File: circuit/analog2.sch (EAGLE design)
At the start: 65 parts, among them IC1 OP07C, IC2 74HC4052D, IC3 OP07C

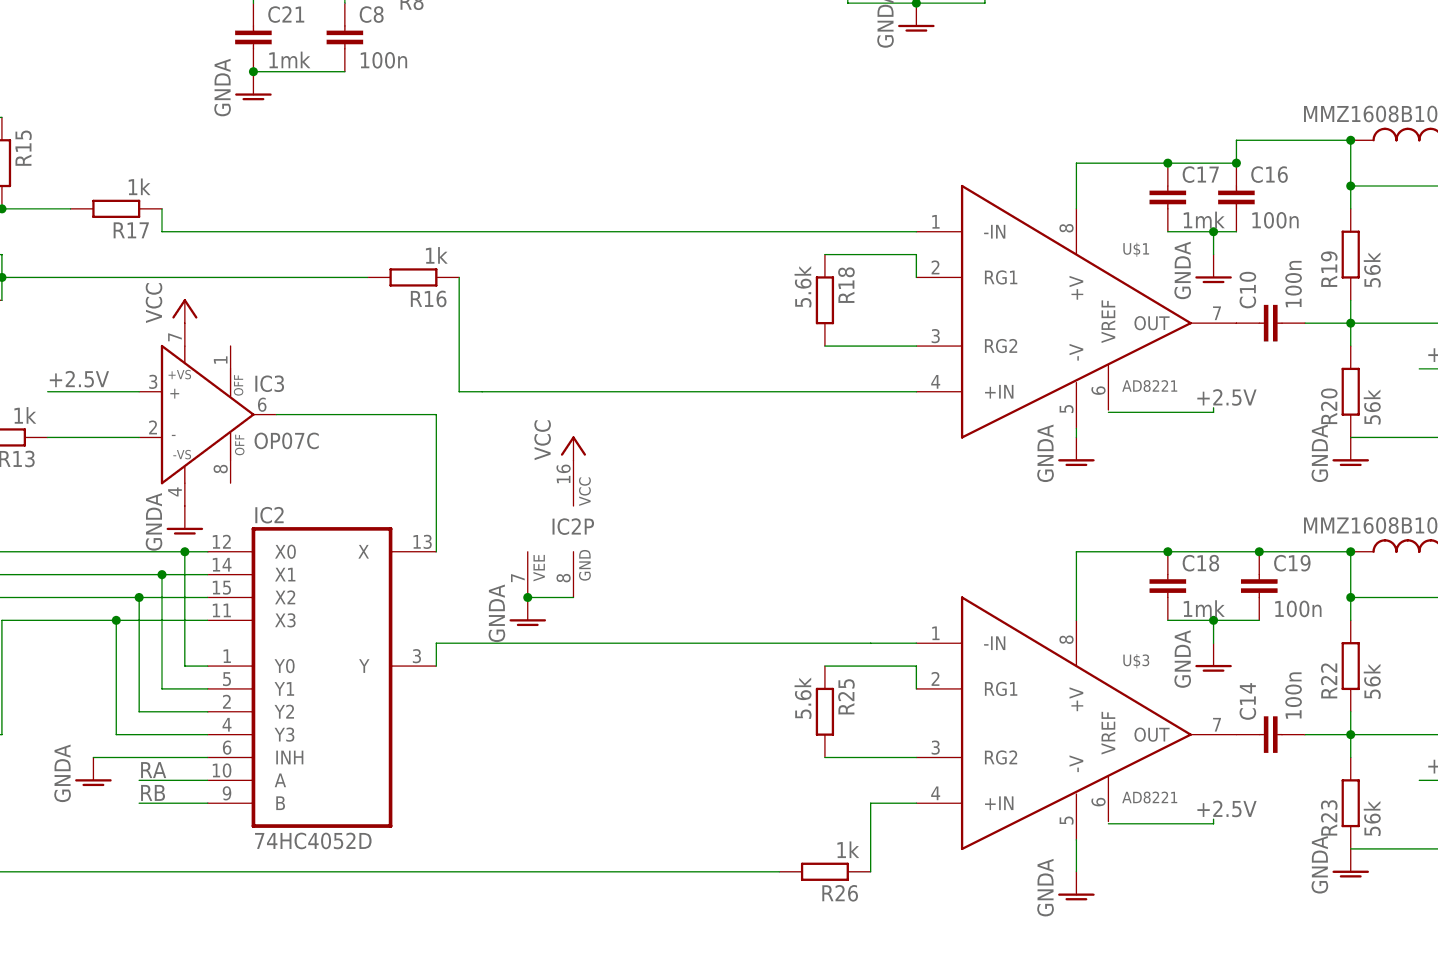
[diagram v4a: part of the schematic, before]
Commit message: - черновой вариант разводки, не проверяли как земля разведенна. Не добавляли пинов, чтобы осциллографом цепляться
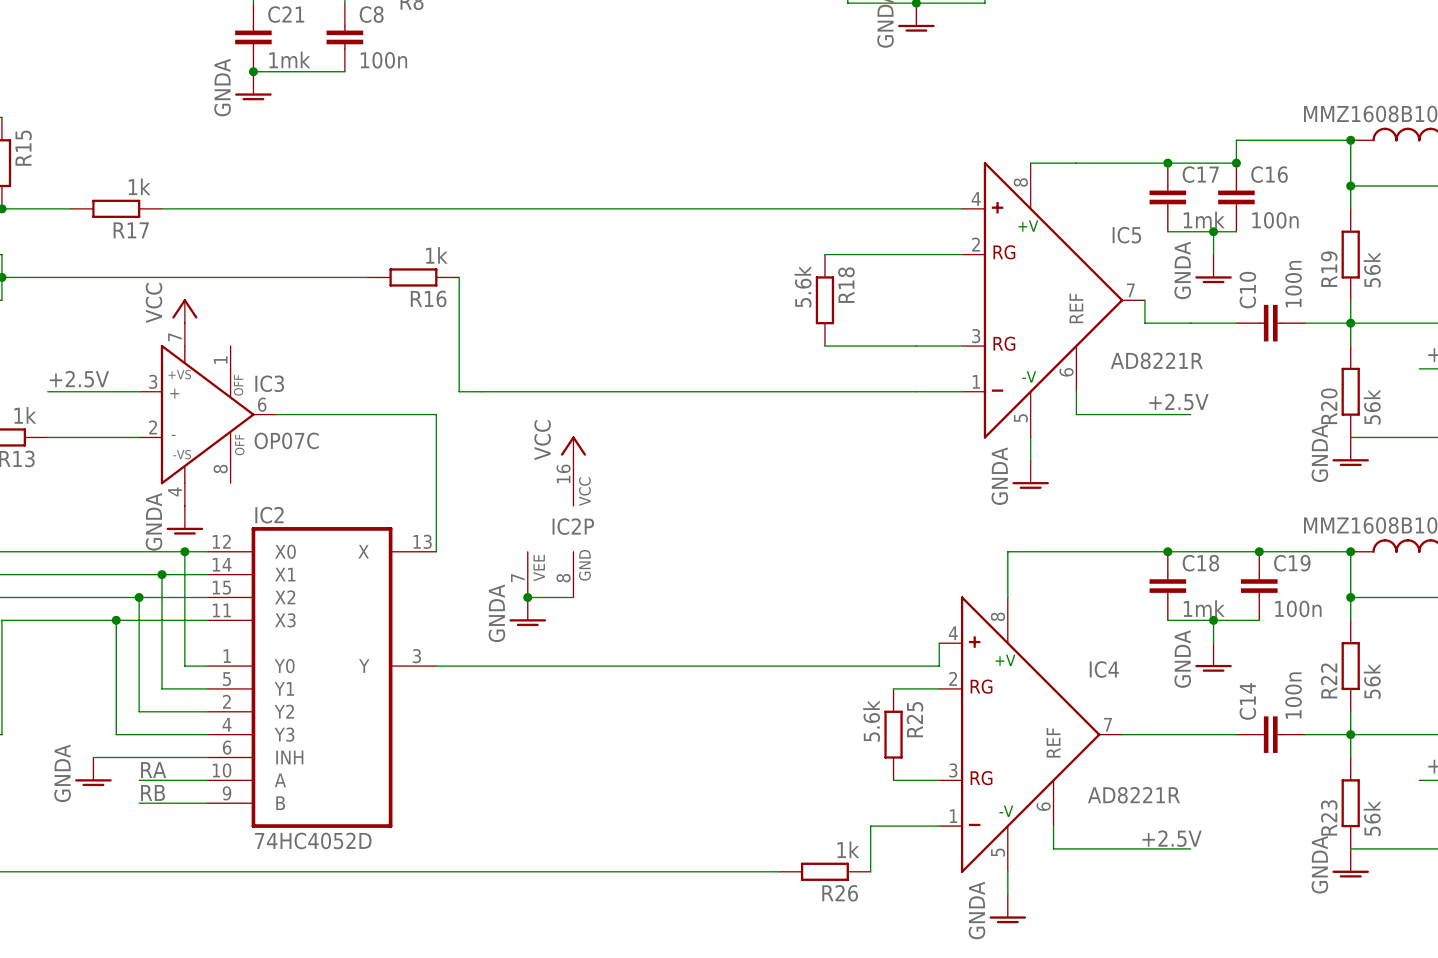
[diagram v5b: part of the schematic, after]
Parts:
- removed U$1, U$3: AD8221, balmer:AD8221
- added IC4, IC5: AD8221R, balmer:AD8221R
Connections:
- removed net I_IN+: R26.1, U$3.+IN
- removed net I_IN-: IC2A.Y, U$3.-IN
- new net N$1: IC5.+, R17.1
- new net N$9: IC4.RG@2, R25.2
- net +2.5V: now also IC4.REF, IC5.REF
- net GNDA: now also IC4.-V, IC5.-V; no longer U$1.-V, U$3.-V
- net N$20: now also IC5.OUT; no longer U$1.OUT
- net N$21: now also IC4.RG@1, R25.1; no longer R25.2, U$3.RG2
- net N$22: now also IC4.-, R26.1; no longer R25.1, U$3.RG1
- net N$23: now also IC5.RG@2; no longer U$1.RG2
- net N$24: now also IC5.RG@1; no longer U$1.RG1
- net N$29: now also IC4.OUT; no longer U$3.OUT
- net N$30: now also IC2A.Y, IC4.+; no longer R17.1, U$1.-IN
- net N$32: now also IC5.+V; no longer U$1.+V
- net N$34: now also IC4.+V; no longer U$3.+V
- net V_IN+: now also IC5.-; no longer U$1.+IN
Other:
- moved on the sheet: R25

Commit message: - пины для теста
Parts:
- added LSP1, LSP2: LSP10, solpad:LSP10
- added X3, X9: 332-02, con-garry:332-02
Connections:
- net N$1: now also X3-2.S
- net N$20: now also LSP1.MP
- net N$22: now also X9-1.S
- net N$29: now also LSP2.MP
- net N$30: now also X9-2.S
- net V_IN+: now also X3-1.S
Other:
- moved on the sheet: R26
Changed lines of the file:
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@@
 <part name="IC4" library="balmer" deviceset="AD8221" device="R"/>
 <part name="IC5" library="balmer" deviceset="AD8221" device="R"/>
+<part name="LSP1" library="solpad" deviceset="LSP10" device=""/>
+<part name="LSP2" library="solpad" deviceset="LSP10" device=""/>
+<part name="X3" library="con-garry" deviceset="332-02" device=""/>
+<part name="X9" library="con-garry" deviceset="332-02" device=""/>
 </parts>
 <sheets>
@@
 <instance part="GND16" gate="1" x="162.56" y="-30.48"/>
 <instance part="R25" gate="G$1" x="55.88" y="-27.94" rot="R270"/>
-<instance part="R26" gate="G$1" x="48.26" y="-43.18" rot="R180"/>
+<instance part="R26" gate="G$1" x="15.24" y="-43.18" rot="R180"/>
 <instance part="L3" gate="G$1" x="114.3" y="38.1" rot="R90"/>
 <instance part="C16" gate="G$1" x="93.98" y="33.02"/>
@@
 <instance part="IC4" gate="G$1" x="68.58" y="-27.94"/>
 <instance part="IC5" gate="G$1" x="71.12" y="20.32"/>
+<instance part="LSP1" gate="1" x="86.36" y="20.32"/>
+<instance part="LSP2" gate="1" x="83.82" y="-25.4"/>
+<instance part="X3" gate="-1" x="25.4" y="15.24"/>
+<instance part="X3" gate="-2" x="25.4" y="25.4"/>
+<instance part="X9" gate="-1" x="25.4" y="-38.1"/>
+<instance part="X9" gate="-2" x="25.4" y="-25.4"/>
 </instances>
 <busses>
@@
 <pinref part="IC5" gate="G$1" pin="OUT"/>
 <wire x1="83.82" y1="20.32" x2="83.82" y2="17.78" width="0.1524" layer="91"/>
-<wire x1="83.82" y1="17.78" x2="88.9" y2="17.78" width="0.1524" layer="91"/>
+<wire x1="83.82" y1="17.78" x2="86.36" y2="17.78" width="0.1524" layer="91"/>
+<pinref part="LSP1" gate="1" pin="MP"/>
+<wire x1="86.36" y1="17.78" x2="88.9" y2="17.78" width="0.1524" layer="91"/>
+<junction x="86.36" y="17.78"/>
 </segment>
 </net>
 <net name="V_IN+" class="0">
 <segment>
-<wire x1="58.42" y1="10.16" x2="10.16" y2="10.16" width="0.1524" layer="91"/>
+<wire x1="58.42" y1="10.16" x2="22.86" y2="10.16" width="0.1524" layer="91"/>
 <pinref part="R16" gate="G$1" pin="1"/>
+<wire x1="22.86" y1="10.16" x2="10.16" y2="10.16" width="0.1524" layer="91"/>
 <wire x1="10.16" y1="10.16" x2="7.62" y2="10.16" width="0.1524" layer="91"/>
 <wire x1="7.62" y1="10.16" x2="7.62" y2="22.86" width="0.1524" layer="91"/>
 <pinref part="IC5" gate="G$1" pin="-"/>
 <wire x1="63.5" y1="10.16" x2="58.42" y2="10.16" width="0.1524" layer="91"/>
+<pinref part="X3" gate="-1" pin="S"/>
+<wire x1="22.86" y1="15.24" x2="22.86" y2="10.16" width="0.1524" layer="91"/>
+<junction x="22.86" y="10.16"/>
 </segment>
 </net>
@@
 <wire x1="-58.42" y1="-35.56" x2="-58.42" y2="-43.18" width="0.1524" layer="91"/>
 <pinref part="R26" gate="G$1" pin="2"/>
-<wire x1="43.18" y1="-43.18" x2="-58.42" y2="-43.18" width="0.1524" layer="91"/>
+<wire x1="10.16" y1="-43.18" x2="-58.42" y2="-43.18" width="0.1524" layer="91"/>
 </segment>
 </net>
@@
 <pinref part="IC5" gate="G$1" pin="+"/>
 <pinref part="R17" gate="G$1" pin="1"/>
-<wire x1="63.5" y1="30.48" x2="-25.4" y2="30.48" width="0.1524" layer="91"/>
+<wire x1="63.5" y1="30.48" x2="22.86" y2="30.48" width="0.1524" layer="91"/>
+<pinref part="X3" gate="-2" pin="S"/>
+<wire x1="22.86" y1="30.48" x2="-25.4" y2="30.48" width="0.1524" layer="91"/>
+<wire x1="22.86" y1="25.4" x2="22.86" y2="30.48" width="0.1524" layer="91"/>
+<junction x="22.86" y="30.48"/>
 </segment>
 </net>
@@
 <segment>
 <pinref part="R26" gate="G$1" pin="1"/>
-<wire x1="53.34" y1="-43.18" x2="53.34" y2="-38.1" width="0.1524" layer="91"/>
+<wire x1="20.32" y1="-43.18" x2="22.86" y2="-43.18" width="0.1524" layer="91"/>
+<wire x1="22.86" y1="-43.18" x2="45.72" y2="-43.18" width="0.1524" layer="91"/>
+<wire x1="45.72" y1="-43.18" x2="45.72" y2="-38.1" width="0.1524" layer="91"/>
+<wire x1="45.72" y1="-38.1" x2="53.34" y2="-38.1" width="0.1524" layer="91"/>
 <pinref part="IC4" gate="G$1" pin="-"/>
 <wire x1="53.34" y1="-38.1" x2="60.96" y2="-38.1" width="0.1524" layer="91"/>
+<pinref part="X9" gate="-1" pin="S"/>
+<wire x1="22.86" y1="-38.1" x2="22.86" y2="-43.18" width="0.1524" layer="91"/>
+<junction x="22.86" y="-43.18"/>
 </segment>
 </net>
@@
 <pinref part="IC2" gate="A" pin="Y"/>
 <pinref part="IC4" gate="G$1" pin="+"/>
-<wire x1="5.08" y1="-20.32" x2="60.96" y2="-20.32" width="0.1524" layer="91"/>
+<wire x1="5.08" y1="-20.32" x2="22.86" y2="-20.32" width="0.1524" layer="91"/>
+<wire x1="22.86" y1="-20.32" x2="60.96" y2="-20.32" width="0.1524" layer="91"/>
 <wire x1="60.96" y1="-20.32" x2="60.96" y2="-17.78" width="0.1524" layer="91"/>
+<pinref part="X9" gate="-2" pin="S"/>
+<wire x1="22.86" y1="-25.4" x2="22.86" y2="-20.32" width="0.1524" layer="91"/>
+<junction x="22.86" y="-20.32"/>
 </segment>
 </net>
@@
 <pinref part="C14" gate="G$1" pin="1"/>
 <pinref part="IC4" gate="G$1" pin="OUT"/>
-<wire x1="93.98" y1="-27.94" x2="81.28" y2="-27.94" width="0.1524" layer="91"/>
-</segment>
-</net>
+<wire x1="93.98" y1="-27.94" x2="83.82" y2="-27.94" width="0.1524" layer="91"/>
+<pinref part="LSP2" gate="1" pin="MP"/>
+<wire x1="83.82" y1="-27.94" x2="81.28" y2="-27.94" width="0.1524" layer="91"/>
+<junction x="83.82" y="-27.94"/>
+</segment>
+</net>

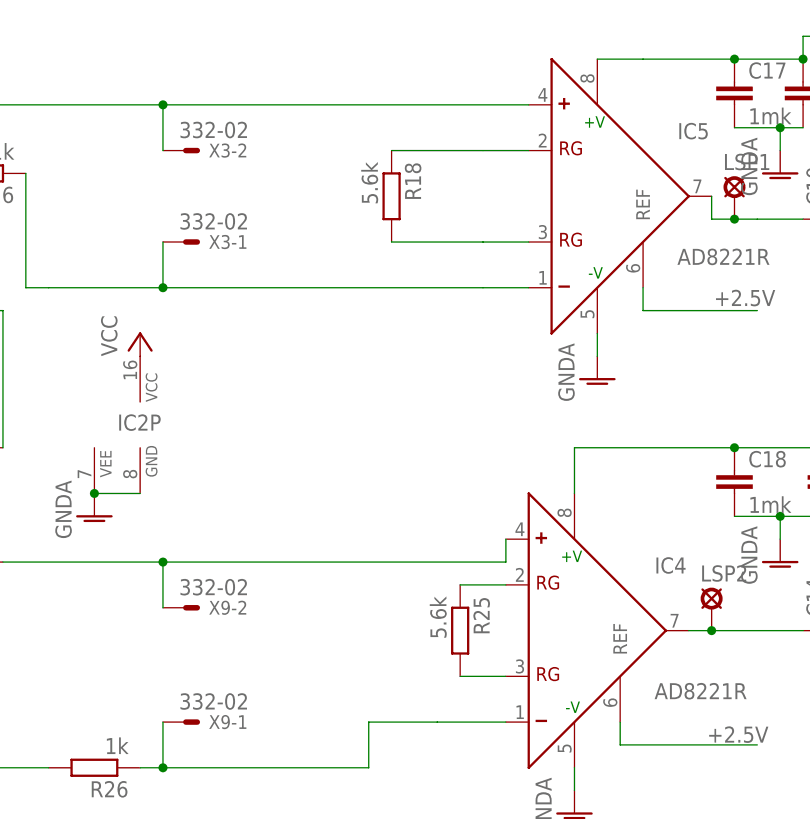
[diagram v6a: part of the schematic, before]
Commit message: - DAC 100 khz STM32F107
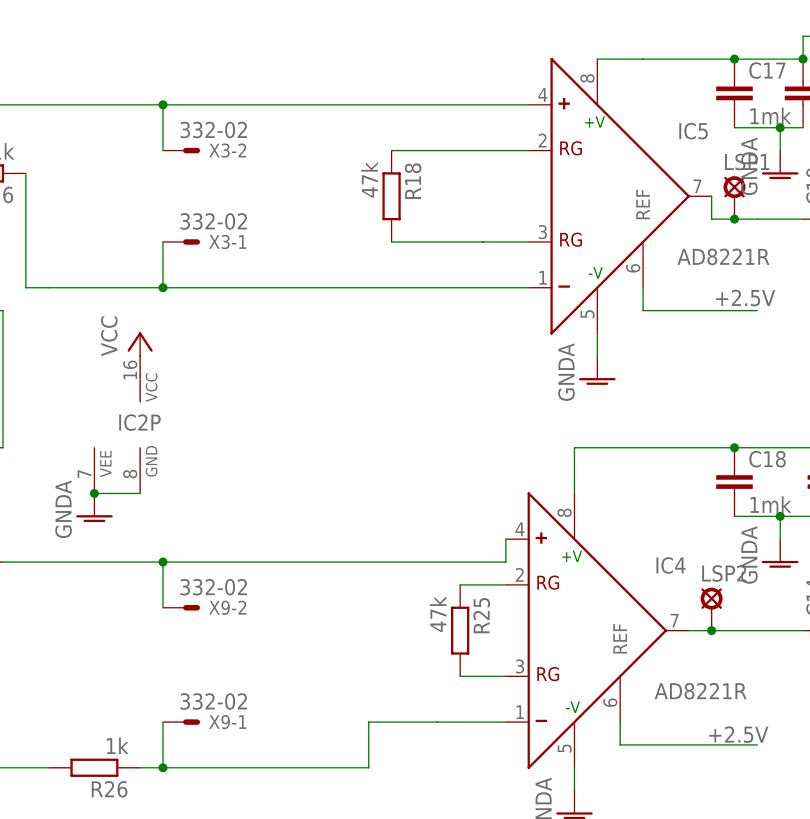
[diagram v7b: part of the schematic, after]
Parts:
- R18, R25: value 5.6k -> 47k
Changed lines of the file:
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@@
 <part name="R17" library="rcl" deviceset="R-EU_" device="R0805" value="1k"/>
 <part name="GND8" library="supply1" deviceset="GNDA" device=""/>
-<part name="R18" library="rcl" deviceset="R-EU_" device="R0805" value="5.6k"/>
+<part name="R18" library="rcl" deviceset="R-EU_" device="R0805" value="47k"/>
 <part name="U$2" library="balmer" deviceset="MCP6S21" device=""/>
 <part name="C10" library="rcl" deviceset="C-EU" device="C0603" value="100n"/>
@@
 <part name="C15" library="rcl" deviceset="C-EU" device="C0805" value="100p"/>
 <part name="GND16" library="supply1" deviceset="GNDA" device=""/>
-<part name="R25" library="rcl" deviceset="R-EU_" device="R0805" value="5.6k"/>
+<part name="R25" library="rcl" deviceset="R-EU_" device="R0805" value="47k"/>
 <part name="R26" library="rcl" deviceset="R-EU_" device="R0805" value="1k"/>
 <part name="L3" library="rcl" deviceset="L-US" device="" value="MMZ1608B102C"/>
